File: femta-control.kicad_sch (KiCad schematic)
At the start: 19 parts, among them J2 CUBESAT INTERFACE

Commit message: work
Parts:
- renumbered J2 to J1, R122 to R1, R15 to R10, R135 to R11, R136 to R12, R133 to R13, R134 to R14, R124 to R2, R125 to R3, R126 to R4, R127 to R5, R12 to R6, R13 to R7, R14 to R8, R139 to R9
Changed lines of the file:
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@@
 		(on_board yes)
 		(dnp no)
-		(property "Reference" "R126"
+		(property "Reference" "R4"
 			(at 107.696 200.66 0)
 			(effects
@@
 			(project "femta-control"
 				(path "/838bf11c-36b7-41d7-9462-fe98a188d617"
-					(reference "R126")
+					(reference "R4")
 					(unit 1)
 				)
@@
 		(on_board yes)
 		(dnp no)
-		(property "Reference" "R122"
+		(property "Reference" "R1"
 			(at 77.47 179.07 0)
 			(effects
@@
 			(project "femta-control"
 				(path "/838bf11c-36b7-41d7-9462-fe98a188d617"
-					(reference "R122")
+					(reference "R1")
 					(unit 1)
 				)
@@
 		(dnp no)
 		(fields_autoplaced yes)
-		(property "Reference" "#PWR0191"
+		(property "Reference" "#PWR01"
 			(at 44.45 123.19 0)
 			(effects
@@
 			(project "femta-control"
 				(path "/838bf11c-36b7-41d7-9462-fe98a188d617"
-					(reference "#PWR0191")
+					(reference "#PWR01")
 					(unit 1)
 				)
@@
 		(on_board yes)
 		(dnp no)
-		(property "Reference" "R136"
+		(property "Reference" "R12"
 			(at 169.926 171.45 0)
 			(effects
@@
 			(project "femta-control"
 				(path "/838bf11c-36b7-41d7-9462-fe98a188d617"
-					(reference "R136")
+					(reference "R12")
 					(unit 1)
 				)
@@
 		(dnp no)
 		(fields_autoplaced yes)
-		(property "Reference" "#PWR033"
+		(property "Reference" "#PWR011"
 			(at 138.43 57.15 0)
 			(effects
@@
 			(project "femta-control"
 				(path "/838bf11c-36b7-41d7-9462-fe98a188d617"
-					(reference "#PWR033")
+					(reference "#PWR011")
 					(unit 1)
 				)
@@
 		(dnp no)
 		(fields_autoplaced yes)
-		(property "Reference" "#PWR030"
+		(property "Reference" "#PWR06"
 			(at 107.95 57.15 0)
 			(effects
@@
 			(project "femta-control"
 				(path "/838bf11c-36b7-41d7-9462-fe98a188d617"
-					(reference "#PWR030")
+					(reference "#PWR06")
 					(unit 1)
 				)
@@
 		(on_board yes)
 		(dnp no)
-		(property "Reference" "#PWR0196"
+		(property "Reference" "#PWR015"
 			(at 168.91 218.44 0)
 			(effects
@@
 			(project "femta-control"
 				(path "/838bf11c-36b7-41d7-9462-fe98a188d617"
-					(reference "#PWR0196")
+					(reference "#PWR015")
 					(unit 1)
 				)
@@
 		(dnp no)
 		(fields_autoplaced yes)
-		(property "Reference" "#PWR031"
+		(property "Reference" "#PWR07"
 			(at 118.11 57.15 0)
 			(effects
@@
 			(project "femta-control"
 				(path "/838bf11c-36b7-41d7-9462-fe98a188d617"
-					(reference "#PWR031")
+					(reference "#PWR07")
 					(unit 1)
 				)
@@
 		(on_board yes)
 		(dnp no)
-		(property "Reference" "#PWR0197"
+		(property "Reference" "#PWR014"
 			(at 168.91 195.58 0)
 			(effects
@@
 			(project "femta-control"
 				(path "/838bf11c-36b7-41d7-9462-fe98a188d617"
-					(reference "#PWR0197")
+					(reference "#PWR014")
 					(unit 1)
 				)
@@
 		(dnp no)
 		(fields_autoplaced yes)
-		(property "Reference" "J2"
+		(property "Reference" "J1"
 			(at 54.61 100.33 0)
 			(effects
@@
 			(project "femta-control"
 				(path "/838bf11c-36b7-41d7-9462-fe98a188d617"
-					(reference "J2")
+					(reference "J1")
 					(unit 1)
 				)
@@
 		(on_board yes)
 		(dnp no)
-		(property "Reference" "R133"
+		(property "Reference" "R13"
 			(at 169.926 200.66 0)
 			(effects
@@
 			(project "femta-control"
 				(path "/838bf11c-36b7-41d7-9462-fe98a188d617"
-					(reference "R133")
+					(reference "R13")
 					(unit 1)
 				)
@@
 		(on_board yes)
 		(dnp no)
-		(property "Reference" "R134"
+		(property "Reference" "R14"
 			(at 169.926 208.28 0)
 			(effects
@@
 			(project "femta-control"
 				(path "/838bf11c-36b7-41d7-9462-fe98a188d617"
-					(reference "R134")
+					(reference "R14")
 					(unit 1)
 				)
@@
 		(dnp no)
 		(fields_autoplaced yes)
-		(property "Reference" "#PWR015"
+		(property "Reference" "#PWR012"
 			(at 168.91 158.75 0)
 			(effects
@@
 			(project "femta-control"
 				(path "/838bf11c-36b7-41d7-9462-fe98a188d617"
-					(reference "#PWR015")
+					(reference "#PWR012")
 					(unit 1)
 				)
@@
 		(on_board yes)
 		(dnp no)
-		(property "Reference" "R14"
+		(property "Reference" "R8"
 			(at 129.794 57.15 0)
 			(effects
@@
 			(project "femta-control"
 				(path "/838bf11c-36b7-41d7-9462-fe98a188d617"
-					(reference "R14")
+					(reference "R8")
 					(unit 1)
 				)
@@
 		(on_board yes)
 		(dnp no)
-		(property "Reference" "R135"
+		(property "Reference" "R11"
 			(at 169.926 163.83 0)
 			(effects
@@
 			(project "femta-control"
 				(path "/838bf11c-36b7-41d7-9462-fe98a188d617"
-					(reference "R135")
+					(reference "R11")
 					(unit 1)
 				)
@@
 		(on_board yes)
 		(dnp no)
-		(property "Reference" "R15"
+		(property "Reference" "R10"
 			(at 139.954 57.15 0)
 			(effects
@@
 			(project "femta-control"
 				(path "/838bf11c-36b7-41d7-9462-fe98a188d617"
-					(reference "R15")
+					(reference "R10")
 					(unit 1)
 				)
@@
 		(on_board yes)
 		(dnp no)
-		(property "Reference" "R13"
+		(property "Reference" "R7"
 			(at 119.634 57.15 0)
 			(effects
@@
 			(project "femta-control"
 				(path "/838bf11c-36b7-41d7-9462-fe98a188d617"
-					(reference "R13")
+					(reference "R7")
 					(unit 1)
 				)
@@
 		(on_board yes)
 		(dnp no)
-		(property "Reference" "#PWR0199"
+		(property "Reference" "#PWR013"
 			(at 168.91 181.61 0)
 			(effects
@@
 			(project "femta-control"
 				(path "/838bf11c-36b7-41d7-9462-fe98a188d617"
-					(reference "#PWR0199")
+					(reference "#PWR013")
 					(unit 1)
 				)
@@
 		(on_board yes)
 		(dnp no)
-		(property "Reference" "#PWR0185"
+		(property "Reference" "#PWR03"
 			(at 106.68 181.61 0)
 			(effects
@@
 			(project "femta-control"
 				(path "/838bf11c-36b7-41d7-9462-fe98a188d617"
-					(reference "#PWR0185")
+					(reference "#PWR03")
 					(unit 1)
 				)
@@
 		(on_board yes)
 		(dnp no)
-		(property "Reference" "R12"
+		(property "Reference" "R6"
 			(at 109.474 57.15 0)
 			(effects
@@
 			(project "femta-control"
 				(path "/838bf11c-36b7-41d7-9462-fe98a188d617"
-					(reference "R12")
+					(reference "R6")
 					(unit 1)
 				)
@@
 		(on_board yes)
 		(dnp no)
-		(property "Reference" "R124"
+		(property "Reference" "R2"
 			(at 107.696 163.83 0)
 			(effects
@@
 			(project "femta-control"
 				(path "/838bf11c-36b7-41d7-9462-fe98a188d617"
-					(reference "R124")
+					(reference "R2")
 					(unit 1)
 				)
@@
 		(on_board yes)
 		(dnp no)
-		(property "Reference" "R139"
+		(property "Reference" "R9"
 			(at 135.89 163.83 0)
 			(effects
@@
 			(project "femta-control"
 				(path "/838bf11c-36b7-41d7-9462-fe98a188d617"
-					(reference "R139")
+					(reference "R9")
 					(unit 1)
 				)
@@
 		(dnp no)
 		(fields_autoplaced yes)
-		(property "Reference" "#PWR032"
+		(property "Reference" "#PWR09"
 			(at 128.27 57.15 0)
 			(effects
@@
 			(project "femta-control"
 				(path "/838bf11c-36b7-41d7-9462-fe98a188d617"
-					(reference "#PWR032")
+					(reference "#PWR09")
 					(unit 1)
 				)
@@
 		(on_board yes)
 		(dnp no)
-		(property "Reference" "#PWR0190"
+		(property "Reference" "#PWR05"
 			(at 106.68 218.44 0)
 			(effects
@@
 			(project "femta-control"
 				(path "/838bf11c-36b7-41d7-9462-fe98a188d617"
-					(reference "#PWR0190")
+					(reference "#PWR05")
 					(unit 1)
 				)
@@
 		(on_board yes)
 		(dnp no)
-		(property "Reference" "R127"
+		(property "Reference" "R5"
 			(at 107.696 208.28 0)
 			(effects
@@
 			(project "femta-control"
 				(path "/838bf11c-36b7-41d7-9462-fe98a188d617"
-					(reference "R127")
+					(reference "R5")
 					(unit 1)
 				)
@@
 		(on_board yes)
 		(dnp no)
-		(property "Reference" "#PWR0187"
+		(property "Reference" "#PWR04"
 			(at 106.68 195.58 0)
 			(effects
@@
 			(project "femta-control"
 				(path "/838bf11c-36b7-41d7-9462-fe98a188d617"
-					(reference "#PWR0187")
+					(reference "#PWR04")
 					(unit 1)
 				)
@@
 		(on_board yes)
 		(dnp no)
-		(property "Reference" "R125"
+		(property "Reference" "R3"
 			(at 107.696 171.45 0)
 			(effects
@@
 			(project "femta-control"
 				(path "/838bf11c-36b7-41d7-9462-fe98a188d617"
-					(reference "R125")
+					(reference "R3")
 					(unit 1)
 				)
@@
 		(on_board yes)
 		(dnp no)
-		(property "Reference" "#PWR0202"
+		(property "Reference" "#PWR010"
 			(at 134.62 163.83 0)
 			(effects
@@
 			(project "femta-control"
 				(path "/838bf11c-36b7-41d7-9462-fe98a188d617"
-					(reference "#PWR0202")
+					(reference "#PWR010")
 					(unit 1)
 				)
@@
 		(dnp no)
 		(fields_autoplaced yes)
-		(property "Reference" "#PWR034"
+		(property "Reference" "#PWR08"
 			(at 124.46 80.01 0)
 			(effects
@@
 			(project "femta-control"
 				(path "/838bf11c-36b7-41d7-9462-fe98a188d617"
-					(reference "#PWR034")
+					(reference "#PWR08")
 					(unit 1)
 				)
@@
 		(on_board yes)
 		(dnp no)
-		(property "Reference" "#PWR0186"
+		(property "Reference" "#PWR02"
 			(at 106.68 158.75 0)
 			(effects
@@
 			(project "femta-control"
 				(path "/838bf11c-36b7-41d7-9462-fe98a188d617"
-					(reference "#PWR0186")
-					(unit 1)
-				)
+					(reference "#PWR02")
+					(unit 1)
+				)

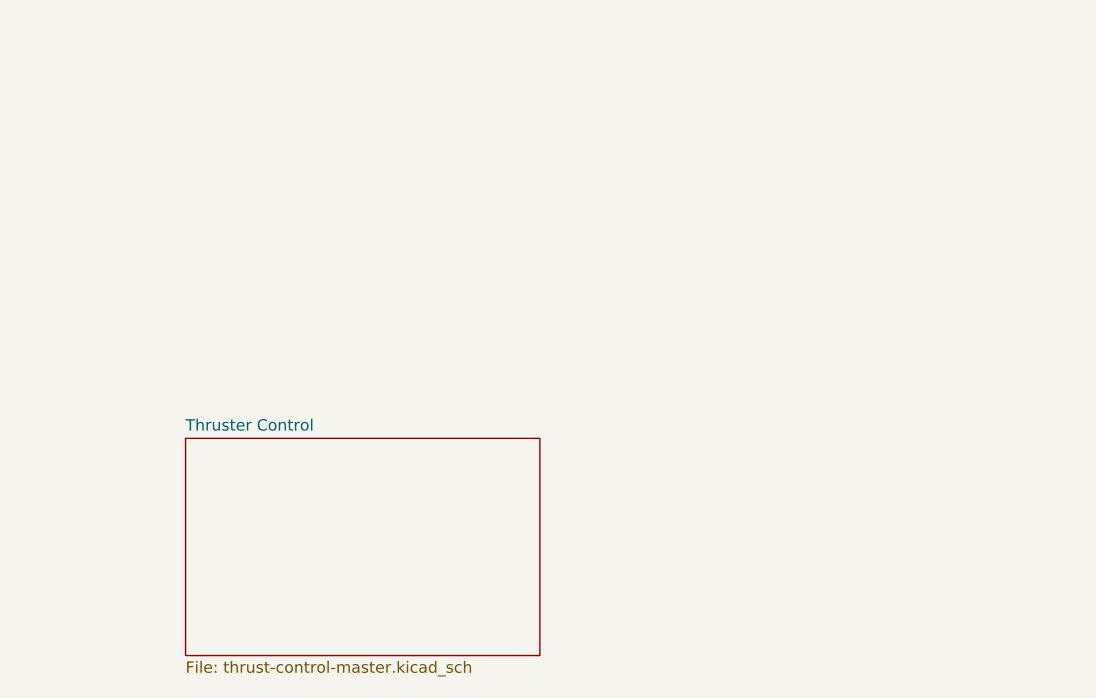
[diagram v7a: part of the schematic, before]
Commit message: thrust control
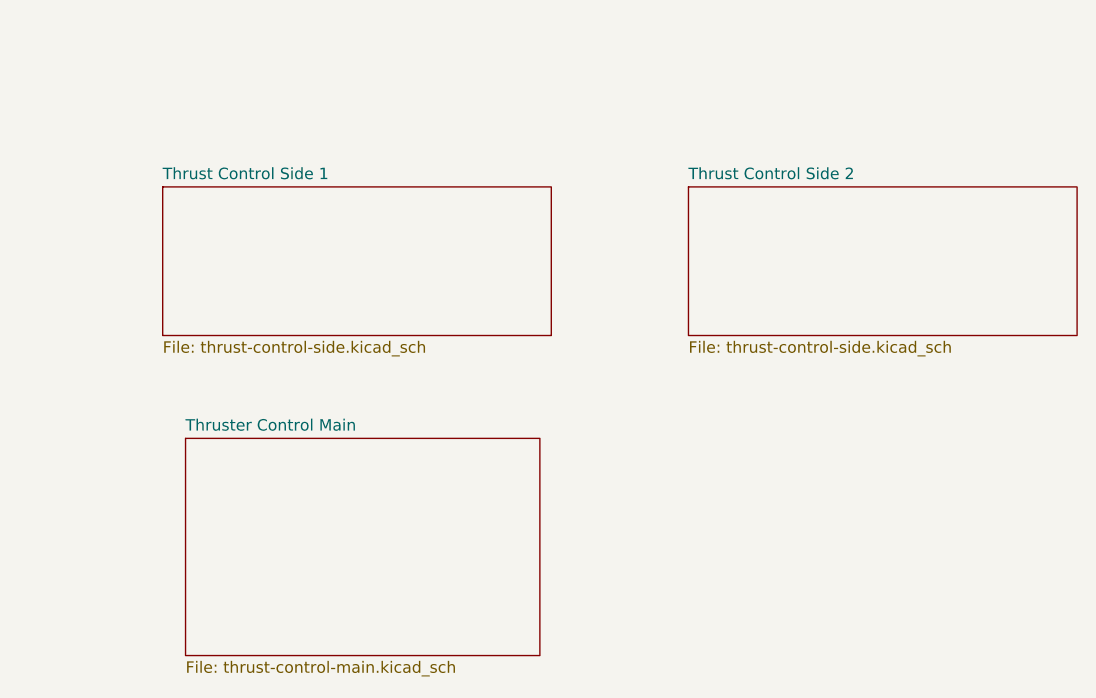
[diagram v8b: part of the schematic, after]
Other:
- sheet Thruster Control renamed Thruster Control Main
- added sheet Thrust Control Side 1 (thrust-control-side.kicad_sch)
- added sheet Thrust Control Side 2 (thrust-control-side.kicad_sch)
- sheet Thruster Control Main: file thrust-control-master.kicad_sch -> thrust-control-main.kicad_sch
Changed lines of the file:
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@@
+	)
+	(sheet
+		(at 236.22 171.45)
+		(size 43.18 16.51)
+		(fields_autoplaced yes)
+		(stroke
+			(width 0.1524)
+			(type solid)
+		)
+		(fill
+			(color 0 0 0 0.0000)
+		)
+		(property "Sheetname" "Thrust Control Side 1"
+			(at 236.22 170.7384 0)
+			(effects
+				(font
+					(size 1.27 1.27)
+				)
+				(justify left bottom)
+			)
+		)
+		(property "Sheetfile" "thrust-control-side.kicad_sch"
+			(at 236.22 188.5446 0)
+			(effects
+				(font
+					(size 1.27 1.27)
+				)
+				(justify left top)
+			)
+		)
+		(instances
+			(project "femta-control"
+				(path "/838bf11c-36b7-41d7-9462-fe98a188d617"
+					(page "29")
+				)
+			)
+		)
 	)
 	(sheet
@@
 			(color 0 0 0 0.0000)
 		)
-		(property "Sheetname" "Thruster Control"
+		(property "Sheetname" "Thruster Control Main"
 			(at 238.76 198.6784 0)
 			(effects
@@
 			)
 		)
-		(property "Sheetfile" "thrust-control-master.kicad_sch"
+		(property "Sheetfile" "thrust-control-main.kicad_sch"
 			(at 238.76 224.1046 0)
 			(effects
@@
 				)
 			)
+		)
+	)
+	(sheet
+		(at 294.64 171.45)
+		(size 43.18 16.51)
+		(fields_autoplaced yes)
+		(stroke
+			(width 0.1524)
+			(type solid)
+		)
+		(fill
+			(color 0 0 0 0.0000)
+		)
+		(property "Sheetname" "Thrust Control Side 2"
+			(at 294.64 170.7384 0)
+			(effects
+				(font
+					(size 1.27 1.27)
+				)
+				(justify left bottom)
+			)
+		)
+		(property "Sheetfile" "thrust-control-side.kicad_sch"
+			(at 294.64 188.5446 0)
+			(effects
+				(font
+					(size 1.27 1.27)
+				)
+				(justify left top)
+			)
+		)
+		(instances
+			(project "femta-control"
+				(path "/838bf11c-36b7-41d7-9462-fe98a188d617"
+					(page "8")
+				)
+			)
